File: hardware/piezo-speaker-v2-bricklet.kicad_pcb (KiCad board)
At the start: 2 copper layers, 49 x 59 mm, 35 parts, among them P1 CON-SENSOR2, P2 BOOT, P3 DEBUG, P4 PT-4532PLQ, U1 XMC1XXX24, U2 LD1117, U3 LMR62014X, U4 DRILL, U5 DRILL, U6 DRILL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

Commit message: changed pcb design
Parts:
- moved R3 7.97 mm to (164.9, 98.7), turned to 180 degrees
- moved C1 6.70 mm to (159.3, 118.8)
- moved RP1 6.63 mm to (157.2, 117.3)
- moved C8 6.59 mm to (140.2, 96.8), turned to 0 degrees
- moved C5 6.48 mm to (145.3, 110.7)
- moved L1 6.13 mm to (146.3, 108.3)
- moved R1 6.05 mm to (161.8, 112.2), turned to 0 degrees
- moved C7 5.83 mm to (145.3, 105.8)
- moved C6 5.66 mm to (169.1, 98.8), turned to 0 degrees
- moved L2 5.32 mm to (145.4, 102.9)
- moved P3 5.30 mm to (159.1, 109.1)
- moved RP2 5.30 mm to (158.3, 102.1)
- moved RP3 5.30 mm to (154.0, 102.1)
- moved RP4 5.30 mm to (150.2, 102.1)
- moved U1 5.30 mm to (155.0, 108.8)
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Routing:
- net GND: track 43.8 -> 55.9 mm, vias 26 -> 28
- net +VSW: track 70.9 -> 82.9 mm
- net 3V3: track 26.3 -> 37.7 mm
- net Net-(D2-Pad1): track 21.5 -> 11.1 mm
- net Net-(D1-Pad2): track 11.6 -> 18.8 mm
- net Net-(C1-Pad1): track 3.21 -> 9.93 mm
- net Net-(P1-Pad6): track 2.97 -> 9.55 mm
- net Net-(P1-Pad5): track 3.29 -> 9.86 mm
- net Net-(P1-Pad4): track 3.92 -> 10.2 mm
- net Net-(C10-Pad1): track 13.0 -> 17.9 mm
- net SU-SHDN: track 20.2 -> 22.2 mm
- net S-MISO: track 12.1 -> 10.5 mm
- net S-CS: track 15.7 -> 14.1 mm
- net S-CLK: track 7.70 -> 6.14 mm
- net S-MOSI: track 7.67 -> 6.14 mm
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
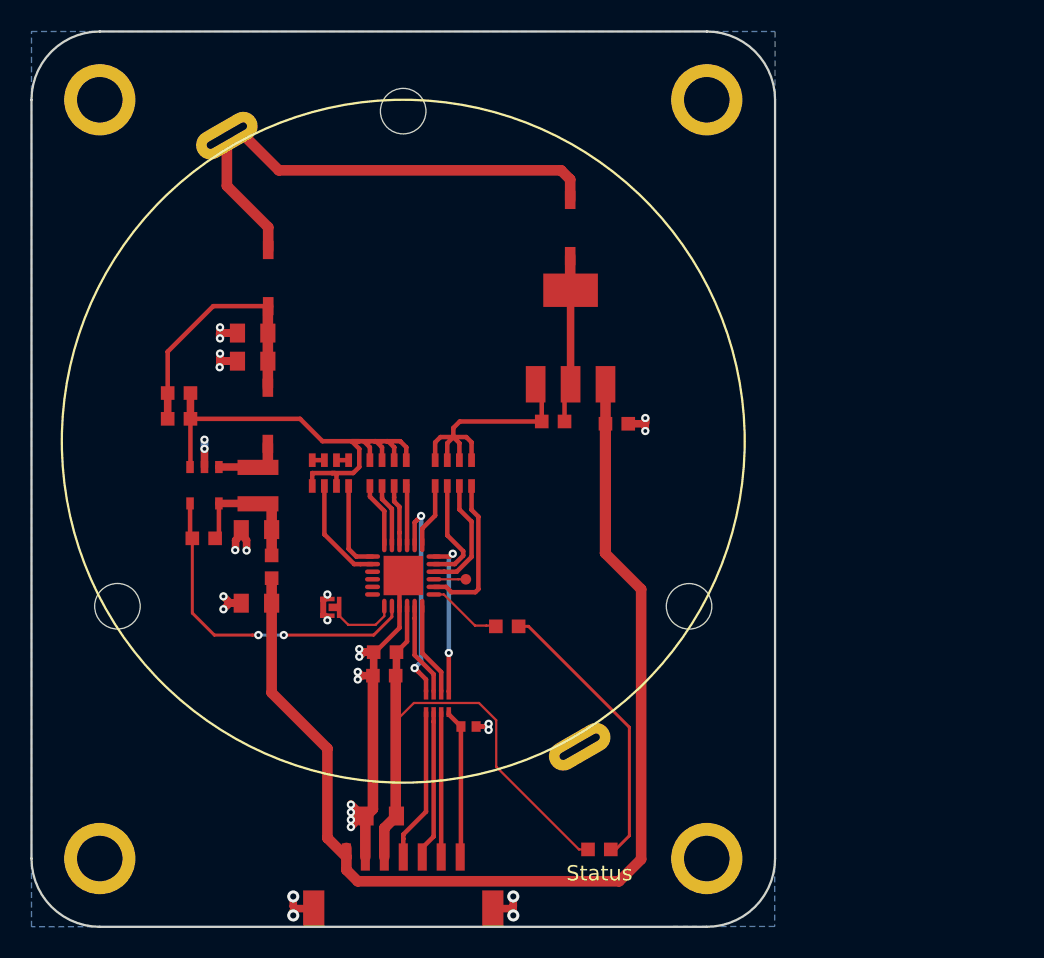
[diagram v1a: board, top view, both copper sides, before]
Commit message: final pcb design (ready for prototype)
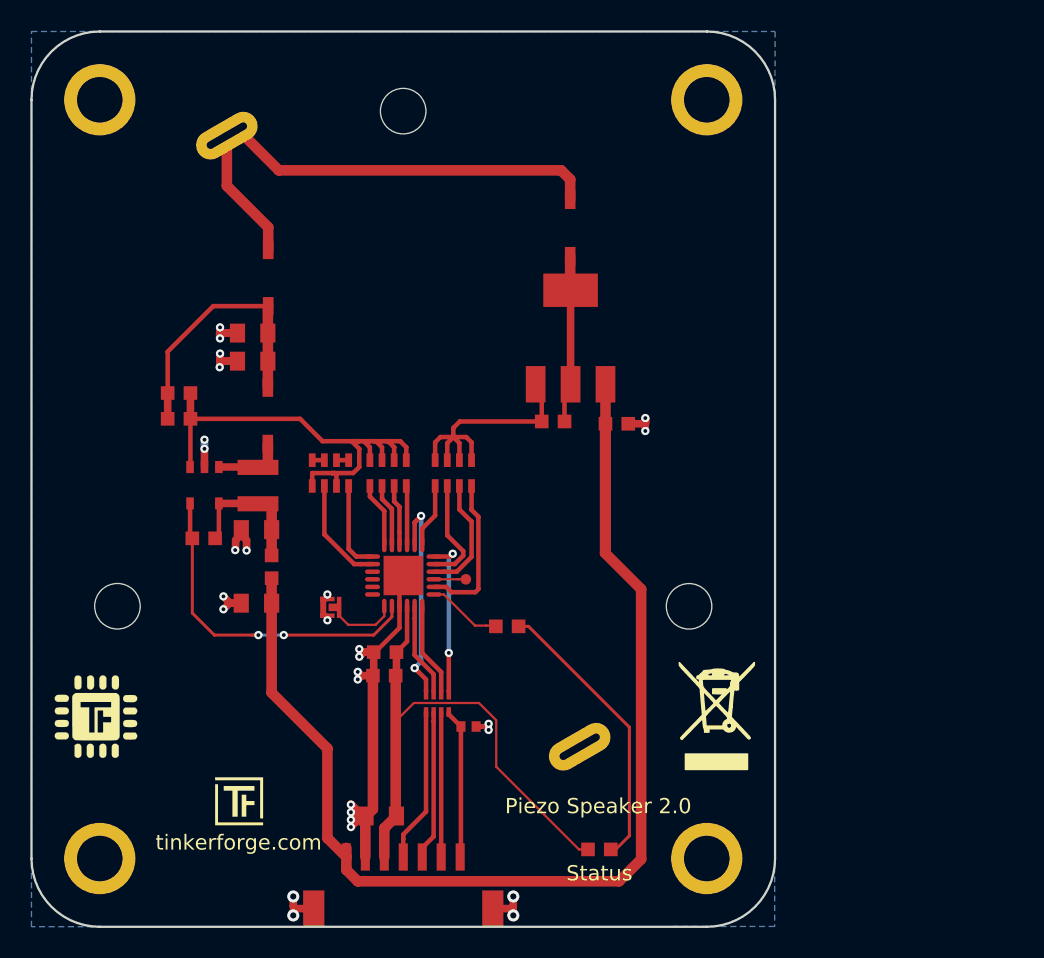
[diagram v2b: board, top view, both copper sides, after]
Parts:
- added G***: LOGO, kicad-libraries:Logo_CoMCU, F.Cu at (134.8, 118.2)
- added G***: Logo_31x31, kicad-libraries:Logo_31x31, F.Cu at (142.6, 122.2)
- added VAL: WEEE_7mm, kicad-libraries:WEEE_7mm, F.Cu at (175.7, 118.1)
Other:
- board text added: "Piezo Speaker 2.0"
- board text added: "tinkerforge.com"

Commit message: improve some fiducials, add text
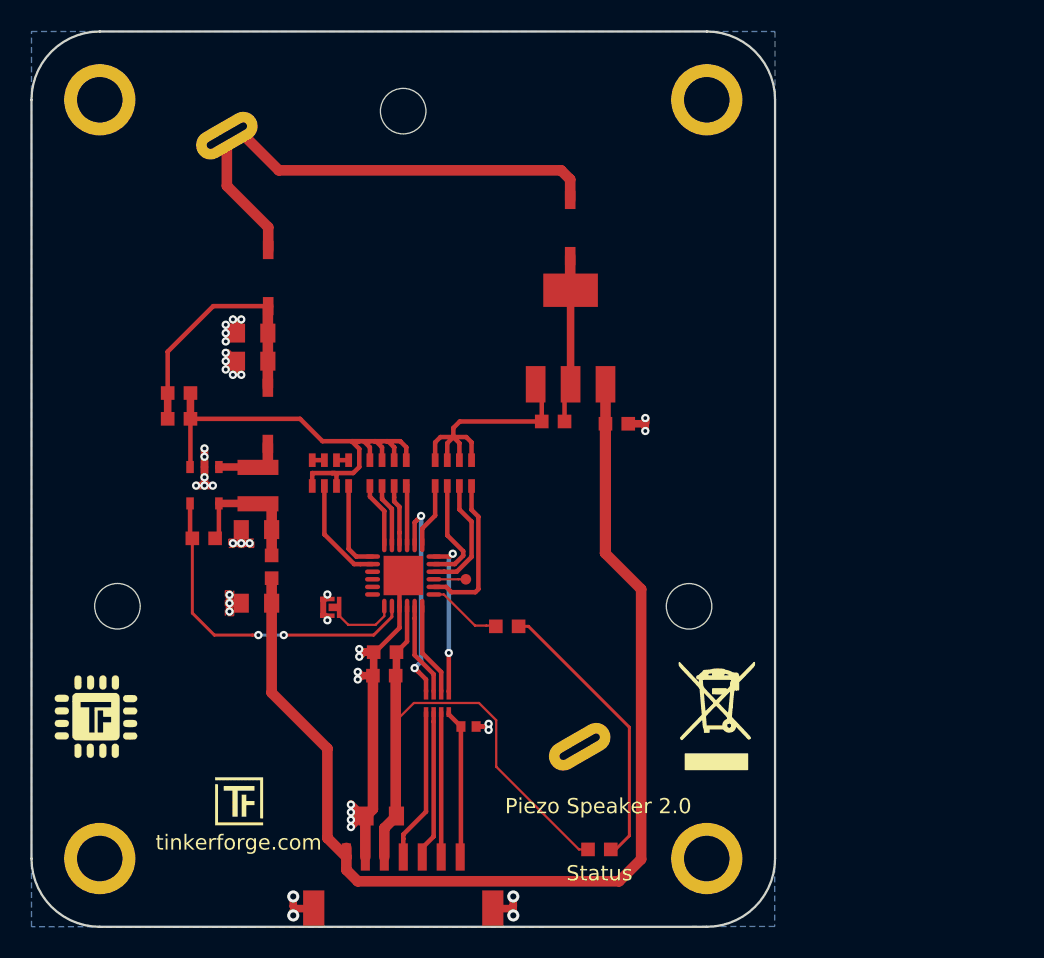
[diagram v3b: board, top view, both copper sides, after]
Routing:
- net GND: track 55.9 -> 58.9 mm, vias 28 -> 40
- added copper zone on F.Cu, net GND
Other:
- board text added: "Copyright Tinkerforge GmbH 2018. This documentation describes Open Hardware and is licensed under the CERN OHL v. 1.1. You may redistribute and modify this documentation under the terms of the CERN OHL v.1.1. (http://ohwr.org/cernohl). This documentation is distributed WITHOUT ANY EXPRESS OR IMPLIED WARRANTY, INCLUDING OF MERCHANTABILITY, SATISFACTORY QUALITY AND FITNESS FOR A PARTICULAR PURPOSE.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"

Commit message: fix outline
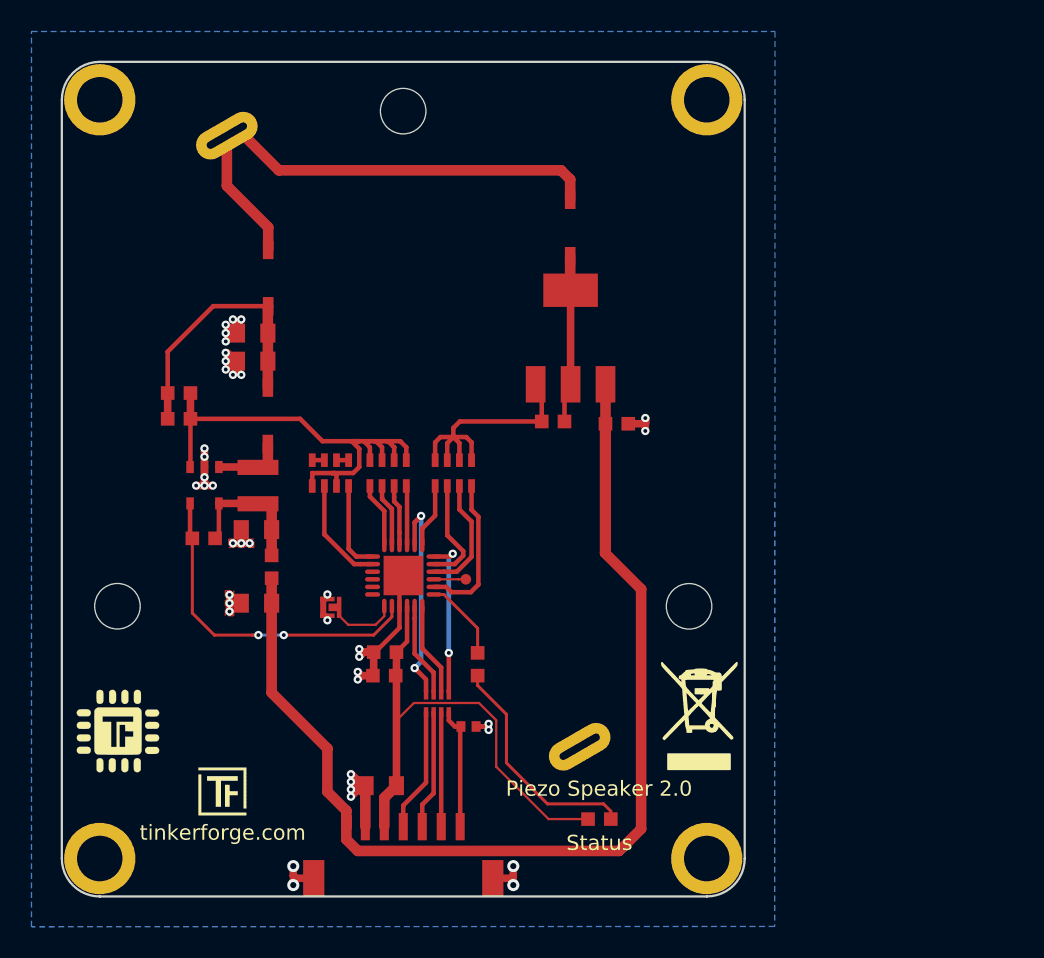
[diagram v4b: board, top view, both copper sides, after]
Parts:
- moved R1 3.17 mm to (159.9, 114.7), turned to 270 degrees
- moved C2 2.00 mm to (153.5, 122.7)
- moved D1 2.00 mm to (167.9, 124.9)
- moved P1 2.00 mm to (155.0, 130.0)
- moved G*** 1.73 mm to (136.2, 119.1)
- moved G*** 1.28 mm to (141.5, 121.5)
- moved VAL 1.15 mm to (174.5, 118.1)
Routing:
- net GND: track 58.9 -> 49.5 mm
- net +VSW: track 82.9 -> 78.9 mm
- net Net-(D1-Pad2): track 18.8 -> 15.3 mm
- net 3V3: track 37.7 -> 34.9 mm
- net Net-(P1-Pad5): track 9.86 -> 7.86 mm
- net Net-(P1-Pad4): track 10.2 -> 8.17 mm
- net Net-(P1-Pad6): track 9.55 -> 7.55 mm
- net Net-(C1-Pad1): track 9.93 -> 8.14 mm
- net Net-(R1-Pad1): track 4.90 -> 6.07 mm
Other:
- board size 49 x 59 mm -> 45 x 55 mm

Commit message: changed the PT footprint, logos, erase and debug pin and first moved the first cap
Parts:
- added VAL: CE_5mm, kicad-libraries:CE_5mm, B.Cu at (162.0, 102.5)
- G***, VAL: moved to B.Cu
- moved VAL 30.8 mm to (148.0, 102.5), turned to 180 degrees
- moved P2 25.9 mm to (174.6, 119.7), turned to 180 degrees
- moved G*** 25.1 mm to (155.0, 102.5), turned to 180 degrees
- moved P3 17.5 mm to (174.6, 117.2)
- moved C2 4.30 mm to (153.5, 118.4)
- moved D1 0.91 mm to (168.1, 125.8)
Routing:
- net GND: track 49.5 -> 82.4 mm, vias 40 -> 45
- net Net-(P2-Pad2): track 5.06 -> 26.8 mm, vias 0 -> 2
- net Net-(P3-Pad1): track 2.10 -> 20.9 mm, vias 0 -> 2
- net Net-(D1-Pad2): track 15.3 -> 16.3 mm
- net 3V3: track 34.9 -> 34.1 mm

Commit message: fix schematic, add 2n7002p, change pins
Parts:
- added Q101: 2N7002P, SOT23GDS, F.Cu at (191.0, 74.5)
- added R101: 1k, R0603F, F.Cu at (194.0, 73.7)
- R2: value 1M -> 1k
- R4: value 118k -> 120k
- RP3: value 1k -> 68k
- RP4: value 1k -> DNP
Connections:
- P4 pad 2: GND -> Net-(P4-Pad2)
- R2 pad 1: Net-(C7-Pad1) -> SU-SHDN
- R2 pad 2: SU-SHDN -> GND
- U1 pad 13: Net-(R1-Pad1) -> Speaker
- U1 pad 3: Net-(U1-Pad3) -> (no net)
- U1 pad 4: Net-(U1-Pad4) -> (no net)
- U1 pad 5: Net-(U1-Pad5) -> (no net)
- U1 pad 6: Net-(U1-Pad6) -> Net-(P2-Pad2)
- U1 pad 7: Net-(P2-Pad2) -> Net-(R1-Pad1)
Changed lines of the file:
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@@
-(kicad_pcb (version 20171130) (host pcbnew 5.0.0-fee4fd1~66~ubuntu16.04.1)
+(kicad_pcb (version 20171130) (host pcbnew 5.0.1-33cea8e~68~ubuntu18.04.1)
   (general
     (thickness 1.6)
@@
     (tracks 449)
     (zones 0)
-    (modules 39)
-    (nets 40)
+    (modules 41)
+    (nets 38)
   )
   (page A4)
@@
   )
   (setup
-    (last_trace_width 0.2)
+    (last_trace_width 0.15)
     (user_trace_width 0.2)
     (user_trace_width 0.25)
@@
     (pad_drill 0.762)
     (pad_to_mask_clearance 0.2)
+    (solder_mask_min_width 0.25)
     (aux_axis_origin 0 0)
     (visible_elements FFFFFF7F)
@@
   (net 34 SU-5)
   (net 35 SU-6)
-  (net 36 "Net-(U1-Pad3)")
-  (net 37 "Net-(U1-Pad4)")
-  (net 38 "Net-(U1-Pad5)")
-  (net 39 "Net-(U1-Pad6)")
+  (net 36 "Net-(P4-Pad2)")
+  (net 37 Speaker)
   (net_class Default "This is the default net class."
     (clearance 0.15)
@@
     (add_net "Net-(P2-Pad2)")
     (add_net "Net-(P3-Pad1)")
+    (add_net "Net-(P4-Pad2)")
     (add_net "Net-(R1-Pad1)")
     (add_net "Net-(R3-Pad2)")
     (add_net "Net-(RP4-Pad1)")
     (add_net "Net-(RP4-Pad3)")
-    (add_net "Net-(U1-Pad3)")
-    (add_net "Net-(U1-Pad4)")
-    (add_net "Net-(U1-Pad5)")
-    (add_net "Net-(U1-Pad6)")
     (add_net S-CLK)
     (add_net S-CS)
@@
     (add_net SU-6)
     (add_net SU-SHDN)
+    (add_net Speaker)
   )
   (module kicad-libraries:PT-4532PLQ (layer F.Cu)
@@
       (net 9 "Net-(D2-Pad2)"))
     (pad 2 thru_hole oval (at -23.25 0 120) (size 2.8 5) (drill oval 1 3) (layers *.Cu *.Mask)
-      (net 1 GND))
+      (net 36 "Net-(P4-Pad2)"))
     (pad "" np_thru_hole circle (at 0 -21.75 120) (size 3 3) (drill 3) (layers *.Cu *.Mask))
     (pad "" np_thru_hole circle (at 18.84 10.87 120) (size 3 3) (drill 3) (layers *.Cu *.Mask))
@@
       (effects (font (size 0.2 0.2) (thickness 0.05)))
     )
-    (fp_text value 1M (at 0.05 -0.375 180) (layer F.Fab)
+    (fp_text value 1k (at 0.05 -0.375 180) (layer F.Fab)
       (effects (font (size 0.2 0.2) (thickness 0.05)))
     )
@@
     (fp_line (start -1.45034 -0.65024) (end 1.45034 -0.65024) (layer F.Fab) (width 0.001))
     (pad 2 smd rect (at 0.75 0 180) (size 0.9 0.9) (layers F.Cu F.Paste F.Mask)
-      (net 18 SU-SHDN))
+      (net 1 GND))
     (pad 1 smd rect (at -0.75 0 180) (size 0.9 0.9) (layers F.Cu F.Paste F.Mask)
-      (net 5 "Net-(C7-Pad1)"))
+      (net 18 SU-SHDN))
     (model Resistors_SMD/R_0603.wrl
       (at (xyz 0 0 0))
@@
       (effects (font (size 0.2 0.2) (thickness 0.05)))
     )
-    (fp_text value 118k (at 0.05 -0.375) (layer F.Fab)
+    (fp_text value 120k (at 0.05 -0.375) (layer F.Fab)
       (effects (font (size 0.2 0.2) (thickness 0.05)))
     )
@@
       (effects (font (size 0.29972 0.29972) (thickness 0.07493)))
     )
-    (fp_text value 1k (at 1.01 -0.02) (layer F.Fab)
+    (fp_text value 68k (at 1.01 -0.02) (layer F.Fab)
       (effects (font (size 0.29972 0.29972) (thickness 0.07493)))
     )
@@
       (effects (font (size 0.29972 0.29972) (thickness 0.07493)))
     )
-    (fp_text value 1k (at 1.01 -0.02) (layer F.Fab)
+    (fp_text value DNP (at 1.01 -0.02) (layer F.Fab)
       (effects (font (size 0.29972 0.29972) (thickness 0.07493)))
     )
@@
     (pad 2 smd oval (at -2.025 -0.75) (size 1 0.3) (layers F.Cu F.Paste F.Mask)
       (net 35 SU-6))
-    (pad 3 smd oval (at -2.025 -0.25) (size 1 0.3) (layers F.Cu F.Paste F.Mask)
-      (net 36 "Net-(U1-Pad3)"))
-    (pad 4 smd oval (at -2.025 0.25) (size 1 0.3) (layers F.Cu F.Paste F.Mask)
-      (net 37 "Net-(U1-Pad4)"))
-    (pad 5 smd oval (at -2.025 0.75) (size 1 0.3) (layers F.Cu F.Paste F.Mask)
-      (net 38 "Net-(U1-Pad5)"))
+    (pad 3 smd oval (at -2.025 -0.25) (size 1 0.3) (layers F.Cu F.Paste F.Mask))
+    (pad 4 smd oval (at -2.025 0.25) (size 1 0.3) (layers F.Cu F.Paste F.Mask))
+    (pad 5 smd oval (at -2.025 0.75) (size 1 0.3) (layers F.Cu F.Paste F.Mask))
     (pad 6 smd oval (at -2.025 1.25) (size 1 0.3) (layers F.Cu F.Paste F.Mask)
-      (net 39 "Net-(U1-Pad6)"))
-    (pad 7 smd oval (at -1.25 2.025 90) (size 1 0.3) (layers F.Cu F.Paste F.Mask)
       (net 15 "Net-(P2-Pad2)"))
+    (pad 7 smd oval (at -1.25 2.025 90) (size 1 0.3) (layers F.Cu F.Paste F.Mask)
+      (net 17 "Net-(R1-Pad1)"))
     (pad 8 smd oval (at -0.75 2.025 90) (size 1 0.3) (layers F.Cu F.Paste F.Mask)
       (net 18 SU-SHDN))
@@
       (net 21 S-MOSI))
     (pad 13 smd oval (at 2.025 1.25) (size 1 0.3) (layers F.Cu F.Paste F.Mask)
-      (net 17 "Net-(R1-Pad1)"))
+      (net 37 Speaker))
     (pad 14 smd oval (at 2.025 0.75) (size 1 0.3) (layers F.Cu F.Paste F.Mask)
       (net 24 LR-1))
@@
       (xy -0.55372 -1.41224) (xy -0.55372 -1.67132)) (layer B.SilkS) (width 0.00254))
   )
+  (module SOT23GDS (layer F.Cu)
+    (at 191.024502 74.4732)
+    (descr "Module CMS SOT23 Transistore EBC")
+    (tags "CMS SOT")
+    (attr smd)
+    (fp_text reference Q101 (at -0.925 0) (layer F.Fab)
+      (effects (font (size 0.2 0.2) (thickness 0.05)))
+    )
+    (fp_text value 2N7002P (at 0.775 0) (layer F.Fab)
+      (effects (font (size 0.2 0.2) (thickness 0.05)))
+    )
+    (fp_line (start -1.524 -0.381) (end 1.524 -0.381) (layer F.Fab) (width 0.001))
+    (fp_line (start 1.524 -0.381) (end 1.524 0.381) (layer F.Fab) (width 0.001))
+    (fp_line (start 1.524 0.381) (end -1.524 0.381) (layer F.Fab) (width 0.001))
+    (fp_line (start -1.524 0.381) (end -1.524 -0.381) (layer F.Fab) (width 0.001))
+    (pad S smd rect (at -0.889 -1.016) (size 0.9144 0.9144) (layers F.Cu F.Paste F.Mask)
+      (net 1 GND))
+    (pad G smd rect (at 0.889 -1.016) (size 0.9144 0.9144) (layers F.Cu F.Paste F.Mask)
+      (net 37 Speaker))
+    (pad D smd rect (at 0 1.016) (size 0.9144 0.9144) (layers F.Cu F.Paste F.Mask)
+      (net 36 "Net-(P4-Pad2)"))
+    (model Housing_SOT_SOD/SOT-23.wrl
+      (at (xyz 0 0 0))
+      (scale (xyz 1 1 1))
+      (rotate (xyz 0 0 180))
+    )
+  )
+  (module R0603F (layer F.Cu)
+    (at 193.990842 73.650741)
+    (attr smd)
+    (fp_text reference R101 (at 0.05 0.225) (layer F.Fab)
+      (effects (font (size 0.2 0.2) (thickness 0.05)))
+    )
+    (fp_text value 1k (at 0.05 -0.375) (layer F.Fab)
+      (effects (font (size 0.2 0.2) (thickness 0.05)))
+    )
+    (fp_line (start -1.45034 -0.65024) (end 1.45034 -0.65024) (layer F.Fab) (width 0.001))
+    (fp_line (start 1.45034 -0.65024) (end 1.45034 0.65024) (layer F.Fab) (width 0.001))
+    (fp_line (start 1.45034 0.65024) (end -1.45034 0.65024) (layer F.Fab) (width 0.001))
+    (fp_line (start -1.45034 0.65024) (end -1.45034 -0.65024) (layer F.Fab) (width 0.001))
+    (pad 1 smd rect (at -0.75 0) (size 0.9 0.9) (layers F.Cu F.Paste F.Mask)
+      (net 9 "Net-(D2-Pad2)"))
+    (pad 2 smd rect (at 0.75 0) (size 0.9 0.9) (layers F.Cu F.Paste F.Mask)
+      (net 36 "Net-(P4-Pad2)"))
+    (model Resistors_SMD/R_0603.wrl
+      (at (xyz 0 0 0))
+      (scale (xyz 1 1 1))
+      (rotate (xyz 0 0 0))
+    )
+  )
   (gr_line (start 132.5 77.5) (end 132.5 127.5) (angle 90) (layer Edge.Cuts) (width 0.15))

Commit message: fix bugs
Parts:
- removed D2, D4: B0520LW-7-F, SOD-123
- removed RP2: 1k, 4X0603
- removed RP4: DNP, 4X0603
- added R102: 1k, R0603F, F.Cu at (148.3, 98.9)
- added R103: 470, R0603F, F.Cu at (148.3, 100.2)
- added R104: 220, R0603F, F.Cu at (148.3, 101.5)
- added R105: 100, R0603F, F.Cu at (148.3, 102.8)
- RP3: value 68k -> 34k
- moved R101 47.7 mm to (167.2, 113.1), turned to 270 degrees
- moved Q101 46.7 mm to (164.9, 113.2)
- moved P2 40.3 mm to (134.3, 116.3)
- moved D1 31.2 mm to (137.1, 121.8)
- moved C6 28.0 mm to (144.0, 111.4)
- moved G*** 25.9 mm to (167.1, 125.3)
- moved U2 24.0 mm to (146.3, 106.8), turned to 270 degrees
- moved R1 23.5 mm to (137.1, 120.4), turned to 0 degrees
- moved R3 23.2 mm to (142.0, 102.8), turned to 0 degrees
- moved C8 19.4 mm to (159.2, 92.8), turned to 270 degrees
- moved R4 18.2 mm to (157.5, 92.8), turned to 270 degrees
- moved C10 17.4 mm to (162.3, 95.4), turned to 0 degrees
- moved C9 17.3 mm to (162.3, 93.6), turned to 0 degrees
- moved R2 15.9 mm to (149.8, 92.7), turned to 270 degrees
- moved U3 15.3 mm to (153.2, 92.7), turned to 90 degrees
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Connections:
- C5 pad 1: +VSW -> Net-(C5-Pad1)
- L1 pad 2: +VSW -> Net-(C5-Pad1)
- P4 pad 1: Net-(D2-Pad2) -> Net-(C10-Pad1)
- R101 pad 1: Net-(D2-Pad2) -> Net-(C10-Pad1)
- R3 pad 1: Net-(D2-Pad1) -> Net-(C5-Pad1)
- U1 pad 1: SU-5 -> SU-SHDN
- U1 pad 14: LR-1 -> SU-1
- U1 pad 16: LR-2 -> SU-2
- U1 pad 17: LR-3 -> SU-3
- U1 pad 19: LR-4 -> SU-4
- U1 pad 2: SU-6 -> (no net)
- U1 pad 21: SU-1 -> LR-1
- U1 pad 22: SU-2 -> LR-2
- U1 pad 23: SU-3 -> LR-3
- U1 pad 24: SU-4 -> LR-4
- U1 pad 8: SU-SHDN -> (no net)
- U2 pad 2: Net-(D2-Pad1) -> Net-(C5-Pad1)
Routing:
- net +VSW: track 78.9 -> 20.2 mm
- net Net-(C10-Pad1): track 17.9 -> 62.3 mm
- net Net-(D2-Pad2): track 33.8 -> 0.00 mm
- net Net-(C5-Pad1): track 0.00 -> 21.7 mm
- net Net-(R1-Pad1): track 6.07 -> 23.1 mm, vias 0 -> 2
- net Net-(D1-Pad2): track 16.3 -> 1.40 mm
- net Net-(C8-Pad2): track 32.8 -> 19.9 mm
- net Net-(D2-Pad1): track 11.1 -> 0.00 mm
- net Speaker: track 0.00 -> 9.98 mm
- net Net-(P4-Pad2): track 0.00 -> 9.09 mm
- net SU-6: track 7.17 -> 0.00 mm
- net SU-5: track 5.93 -> 0.00 mm
- net SU-1: track 4.05 -> 9.96 mm
- net GND: track 82.4 -> 87.3 mm, vias 45 -> 49
- net SU-2: track 4.02 -> 7.88 mm
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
